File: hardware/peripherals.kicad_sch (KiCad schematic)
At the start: 0 parts

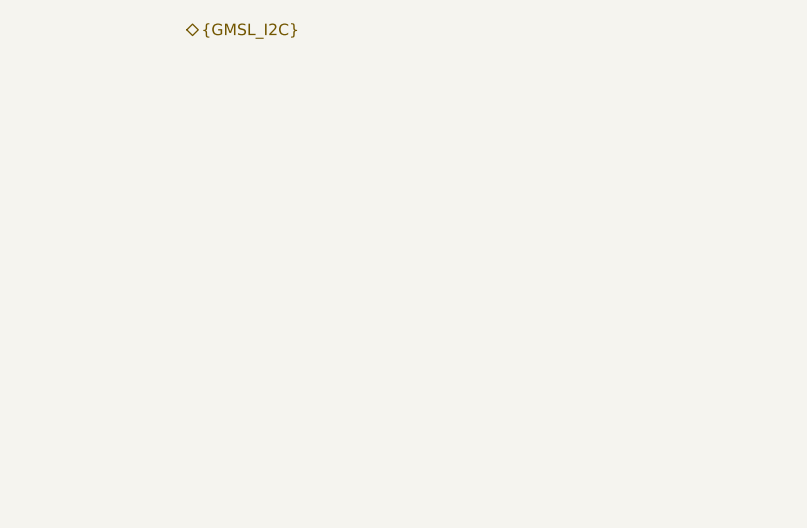
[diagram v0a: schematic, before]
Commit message: started power, added smt fakra
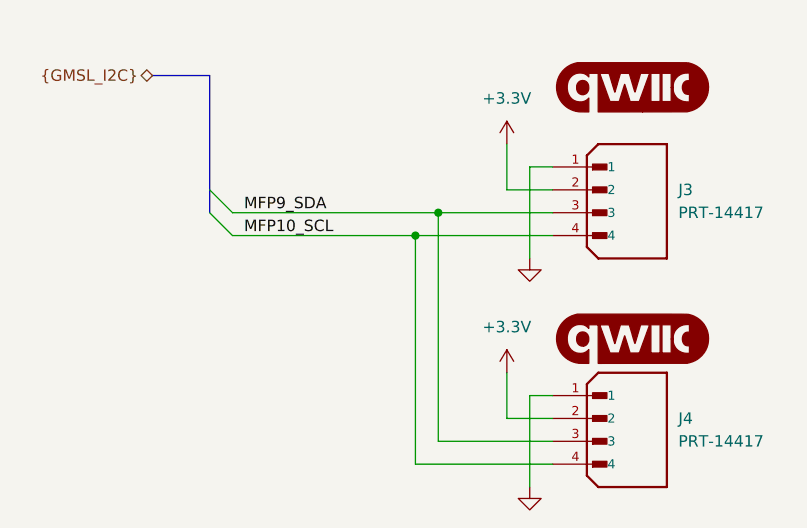
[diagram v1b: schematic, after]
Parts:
- added G1, G2: qwiic_Logo, user:qwiic_3mm, symbol user:qwiic_Logo
- added J3, J4: PRT-14417, user:SPARKFUN_PRT-14417, symbol user:PRT-14417
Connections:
- new net +3.3V: J3.2, J4.2
- new net GND: J3.1, J4.1
- new net MFP10_SCL: J3.4, J4.4
- new net MFP9_SDA: J3.3, J4.3

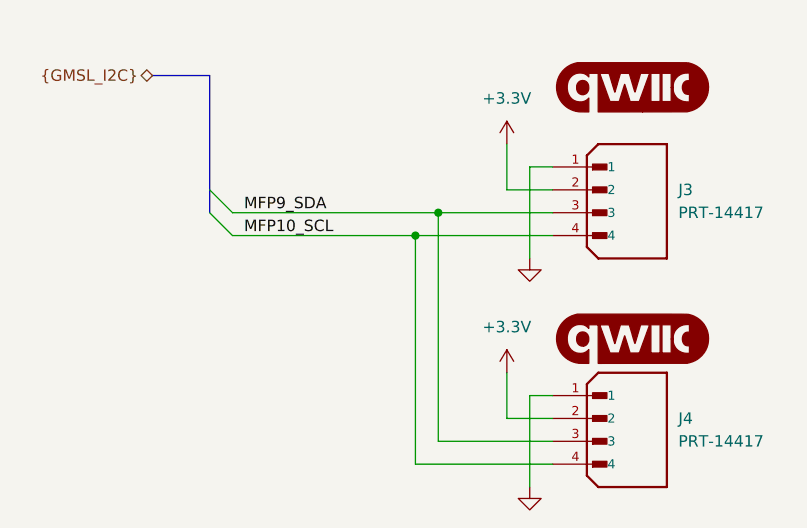
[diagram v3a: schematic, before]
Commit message: cleaned up power supply and started minor power plane routing
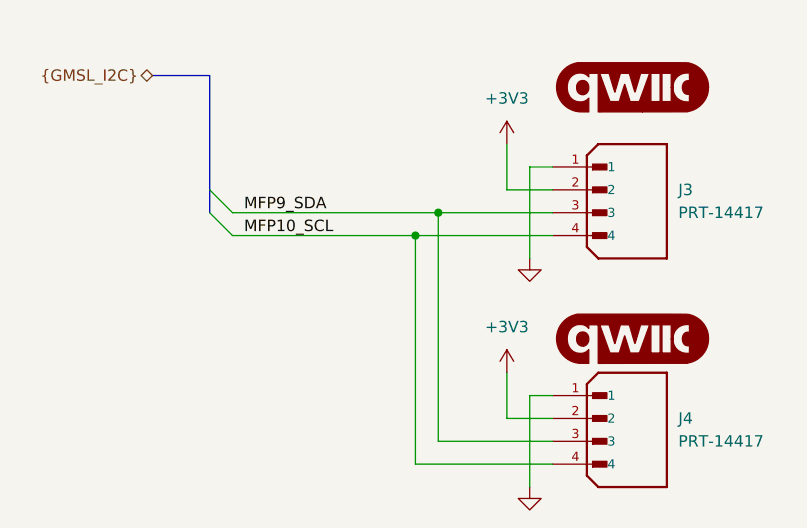
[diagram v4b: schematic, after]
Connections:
- net +3.3V renamed +3V3
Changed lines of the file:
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@@
 			)
 		)
-		(property "Value" "+3.3V"
+		(property "Value" "+3V3"
 			(at 160.02 71.12 0)
 			(effects
@@
 			)
 		)
-		(property "Value" "+3.3V"
+		(property "Value" "+3V3"
 			(at 160.02 96.52 0)
 			(effects

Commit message: prepping for fab
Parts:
- removed G1, G2: qwiic_Logo, user:qwiic_3mm, symbol user:qwiic_Logo
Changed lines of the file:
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@@
-	)
-	(symbol
-		(lib_id "user:qwiic_Logo")
-		(at 173.99 97.79 0)
-		(unit 1)
-		(exclude_from_sim no)
-		(in_bom yes)
-		(on_board no)
-		(dnp no)
-		(fields_autoplaced yes)
-		(property "Reference" "G2"
-			(at 173.99 93.98 0)
-			(effects
-				(font
-					(size 1.27 1.27)
-				)
-				(hide yes)
-			)
-		)
-		(property "Value" "qwiic_Logo"
-			(at 173.99 101.6 0)
-			(effects
-				(font
-					(size 1.27 1.27)
-				)
-				(hide yes)
-			)
-		)
-		(property "Footprint" "user:qwiic_3mm"
-			(at 173.99 104.14 0)
-			(effects
-				(font
-					(size 1.27 1.27)
-				)
-				(hide yes)
-			)
-		)
-		(property "Datasheet" ""
-			(at 173.99 97.79 0)
-			(effects
-				(font
-					(size 1.27 1.27)
-				)
-				(hide yes)
-			)
-		)
-		(property "Description" ""
-			(at 173.99 97.79 0)
-			(effects
-				(font
-					(size 1.27 1.27)
-				)
-				(hide yes)
-			)
-		)
-		(instances
-			(project ""
-				(path "/d9b03904-3e0d-40cc-bc70-bbd63756773a/20d2129d-2f03-433f-9e29-6de838a8fe3e"
-					(reference "G2")
-					(unit 1)
-				)
-			)
-		)
 	)
 	(symbol
@@
 					(unit 1)
 				)
-			)
-		)
-	)
-	(symbol
-		(lib_id "user:qwiic_Logo")
-		(at 173.99 69.85 0)
-		(unit 1)
-		(exclude_from_sim no)
-		(in_bom yes)
-		(on_board no)
-		(dnp no)
-		(fields_autoplaced yes)
-		(property "Reference" "G1"
-			(at 173.99 66.04 0)
-			(effects
-				(font
-					(size 1.27 1.27)
-				)
-				(hide yes)
-			)
-		)
-		(property "Value" "qwiic_Logo"
-			(at 173.99 73.66 0)
-			(effects
-				(font
-					(size 1.27 1.27)
-				)
-				(hide yes)
-			)
-		)
-		(property "Footprint" "user:qwiic_3mm"
-			(at 173.99 76.2 0)
-			(effects
-				(font
-					(size 1.27 1.27)
-				)
-				(hide yes)
-			)
-		)
-		(property "Datasheet" ""
-			(at 173.99 69.85 0)
-			(effects
-				(font
-					(size 1.27 1.27)
-				)
-				(hide yes)
-			)
-		)
-		(property "Description" ""
-			(at 173.99 69.85 0)
-			(effects
-				(font
-					(size 1.27 1.27)
-				)
-				(hide yes)
-			)
-		)
-		(instances
-			(project ""
-				(path "/d9b03904-3e0d-40cc-bc70-bbd63756773a/20d2129d-2f03-433f-9e29-6de838a8fe3e"
-					(reference "G1")
-					(unit 1)
-				)
